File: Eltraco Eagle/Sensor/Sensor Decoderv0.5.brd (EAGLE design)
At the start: 100 x 80 mm, 58 parts

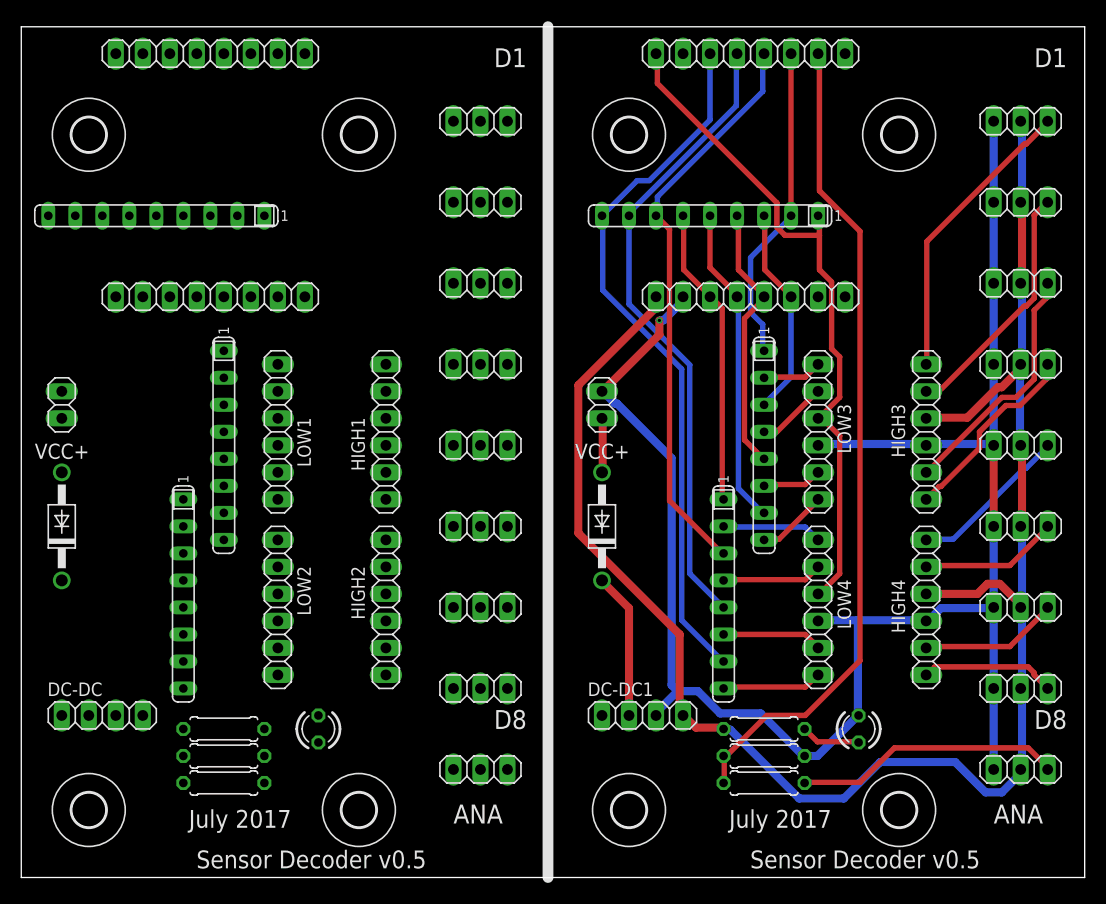
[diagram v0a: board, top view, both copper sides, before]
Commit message: One of two no PCB traces. Corrected.
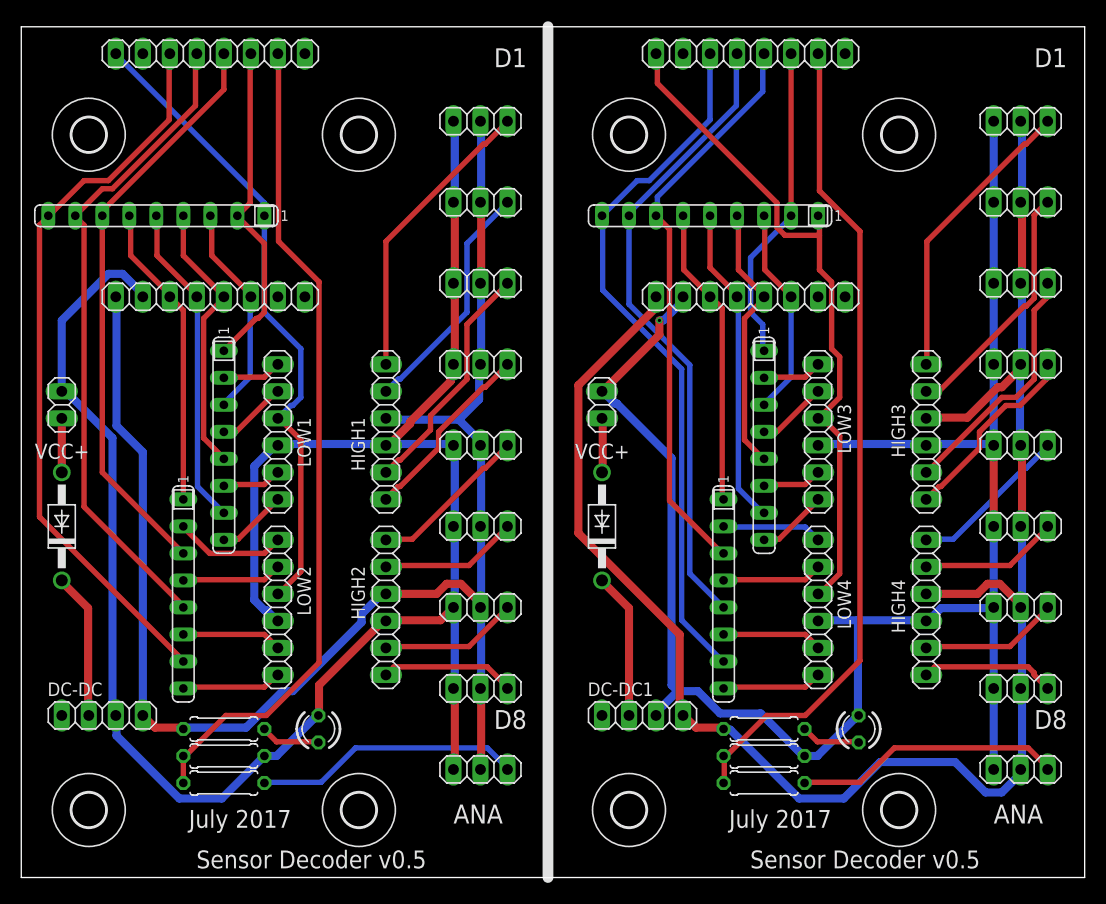
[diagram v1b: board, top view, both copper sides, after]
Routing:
- net PE: track 0.00 -> 195.4 mm
- net +5V: track 0.00 -> 150.0 mm
- net N$58: track 0.00 -> 77.8 mm
- net N$11: track 0.00 -> 69.2 mm
- net N$3: track 0.00 -> 61.6 mm
- net +3V3: track 0.00 -> 61.0 mm
- net N$5: track 0.00 -> 54.9 mm
- net N$2: track 0.00 -> 31.2 mm
- net N$13: track 0.00 -> 30.6 mm
- net N$9: track 0.00 -> 28.9 mm
- net N$17: track 0.00 -> 27.7 mm
- net N$7: track 0.00 -> 26.0 mm
- net N$62: track 0.00 -> 25.2 mm
- net N$15: track 0.00 -> 22.6 mm
- net N$16: track 0.00 -> 22.6 mm
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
